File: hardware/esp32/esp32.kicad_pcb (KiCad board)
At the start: 4 copper layers, 60.8 x 36.3 mm, 149 parts, among them J1 PlugIn_Terminal_Screw, J2 ESP_left, J3 ESP_right, J4 PlugIn_Terminal_01x02, Q1 MMBT5401, Q2 MMBT2222A, U2 LMV321, U3 LMV321, U5 ES8374, U6 LM393, U7 AMS1117-3.3

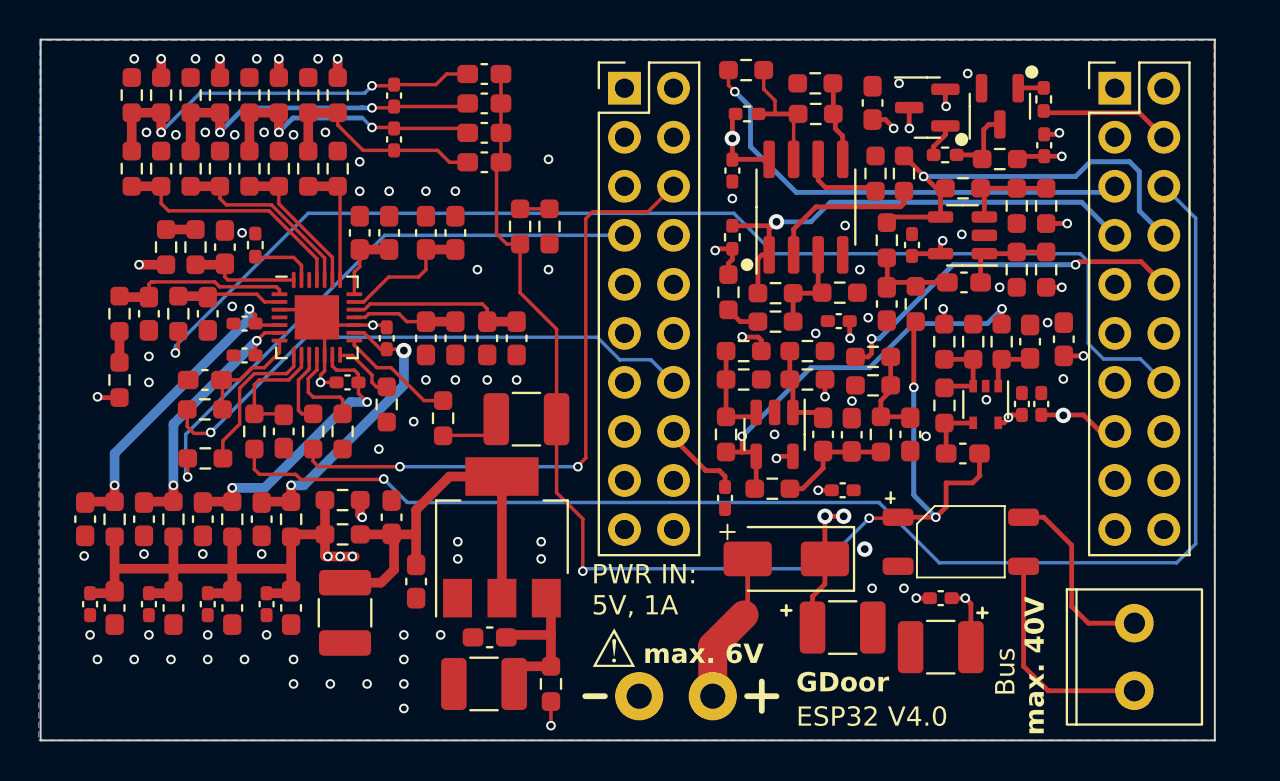
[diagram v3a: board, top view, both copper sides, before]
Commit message: Add production data for first audio try (v4.0)
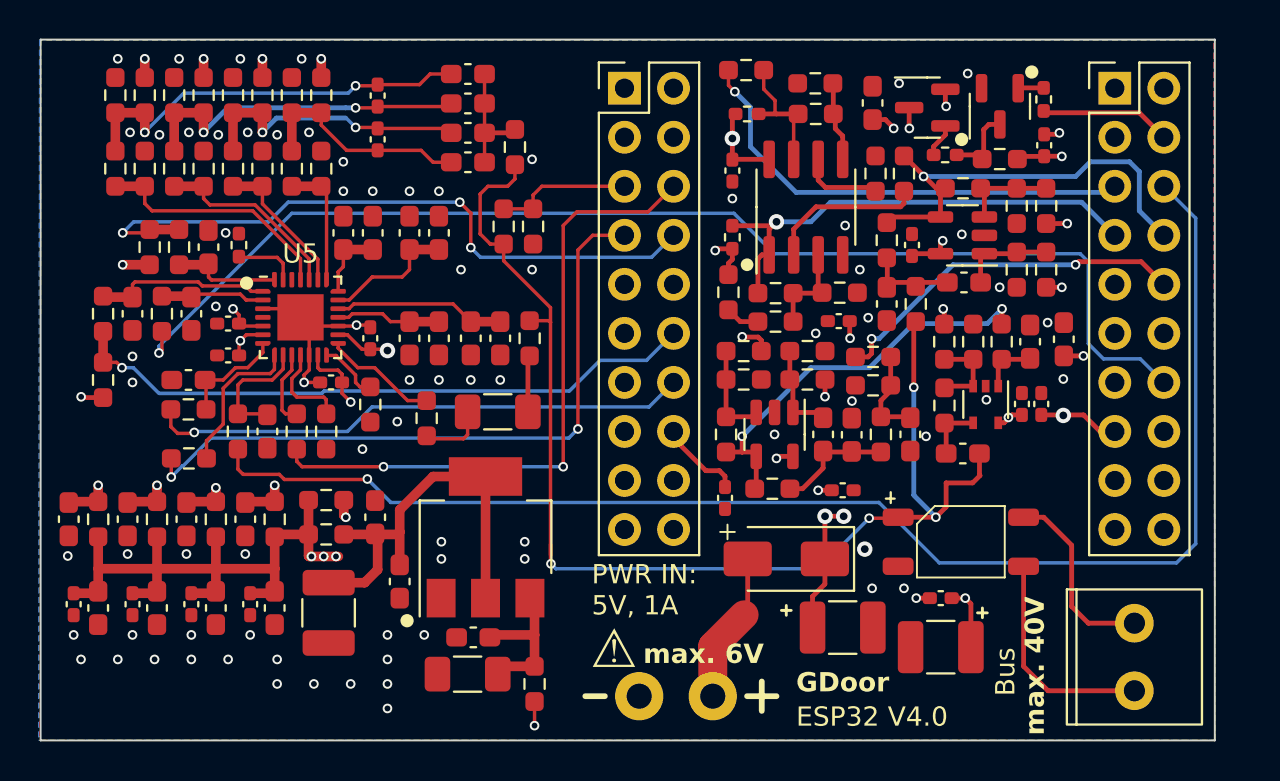
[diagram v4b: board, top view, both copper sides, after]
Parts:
- added R36: 0, Library:R_0603_1608Metric_Pad0.98x0.95mm_HandSolder, F.Cu at (109.4, 93.2)
- added R74: 0, Library:R_0603_1608Metric_Pad0.98x0.95mm_HandSolder, F.Cu at (108.6, 83.3)
- C21: value 100u TBD check voltage -> 10u; footprint Library:C_1210_3225Metric_Pad1.33x2.70mm_HandSolder -> Library:C_1206_3216Metric_Pad1.33x1.80mm_HandSolder
- C57: value 100u -> 10u; footprint Library:C_1210_3225Metric_Pad1.33x2.70mm_HandSolder -> Library:C_1206_3216Metric_Pad1.33x1.80mm_HandSolder
- U5: footprint Library:QFN-28-1EP_4x4mm_P0.4mm_EP2.3x2.3mm -> Library:QFN-28-1EP_4x4mm_P0.45mm_EP2.4x2.4mm
- moved C21 1.53 mm to (107.7, 97.0)
- moved C57 0.99 mm to (106.2, 110.6), turned to 0 degrees
- moved C23 0.85 mm to (104.7, 87.8)
- moved C24 0.85 mm to (103.2, 87.8)
- moved C27 0.85 mm to (104.7, 93.2)
- moved C34 0.85 mm to (103.2, 93.2)
- moved C35 0.85 mm to (101.3, 87.8)
- moved C43 0.85 mm to (94.7, 102.6)
- moved C44 0.85 mm to (88.8, 91.9)
- moved C46 0.85 mm to (85.8, 107.0)
- moved C49 0.85 mm to (95.8, 98.0)
- moved C51 0.85 mm to (88.8, 107.0)
- moved C54 0.85 mm to (93.1, 107.2)
- moved C56 0.85 mm to (96.2, 107.2)
- moved R41 0.85 mm to (96.2, 102.6)
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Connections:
- C21 pad 2: Net-(D1-+) -> Net-(C21-Pad2)
- C28 pad 2: Net-(D1-+) -> Net-(C28-Pad2)
- C29 pad 2: Net-(D1-+) -> Net-(C28-Pad2)
- C30 pad 2: Net-(D1-+) -> Net-(C28-Pad2)
- C31 pad 2: Net-(D1-+) -> Net-(C28-Pad2)
- C57 pad 1: Net-(U7-VI) -> GND
- C57 pad 2: GND -> Net-(U7-VI)
- J2 pad 12: unconnected-(J2-IO_23/D7-Pad12) -> /I2C_SCLK
- J2 pad 5: unconnected-(J2-IO_39/SVN-Pad5) -> /BUS_DCVOLT
- J2 pad 8: unconnected-(J2-IO_18/D5-Pad8) -> /I2C_SDA
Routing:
- net /I2C_SDA: track 1.52 -> 34.9 mm, vias 0 -> 3
- net /I2C_SCLK: track 1.60 -> 33.1 mm, vias 0 -> 1
- net Net-(C28-Pad2): track 0.00 -> 6.85 mm
- net /BUS_DCVOLT: track 1.52 -> 7.16 mm
- net /I2S_ASDOUT: track 30.3 -> 35.1 mm, vias 1 -> 2
- net Net-(C21-Pad2): track 0.00 -> 2.93 mm
- net /I2S_SCLK: track 29.3 -> 28.2 mm
- net Net-(D1-+): track 63.6 -> 62.5 mm
- net /I2S_DSDIN: track 32.7 -> 33.6 mm
- net /I2S_LRCK: track 71.5 -> 72.3 mm
- net /I2S_MCLK: track 61.7 -> 62.6 mm
- net +3.3V: track 22.8 -> 23.7 mm
- net Net-(U5D-AVDD): track 15.1 -> 15.6 mm
